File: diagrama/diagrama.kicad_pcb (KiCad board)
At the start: 2 copper layers, 160 x 101.6 mm, 13 parts, among them J1 Conn_01x02, U1 LM337_TO3

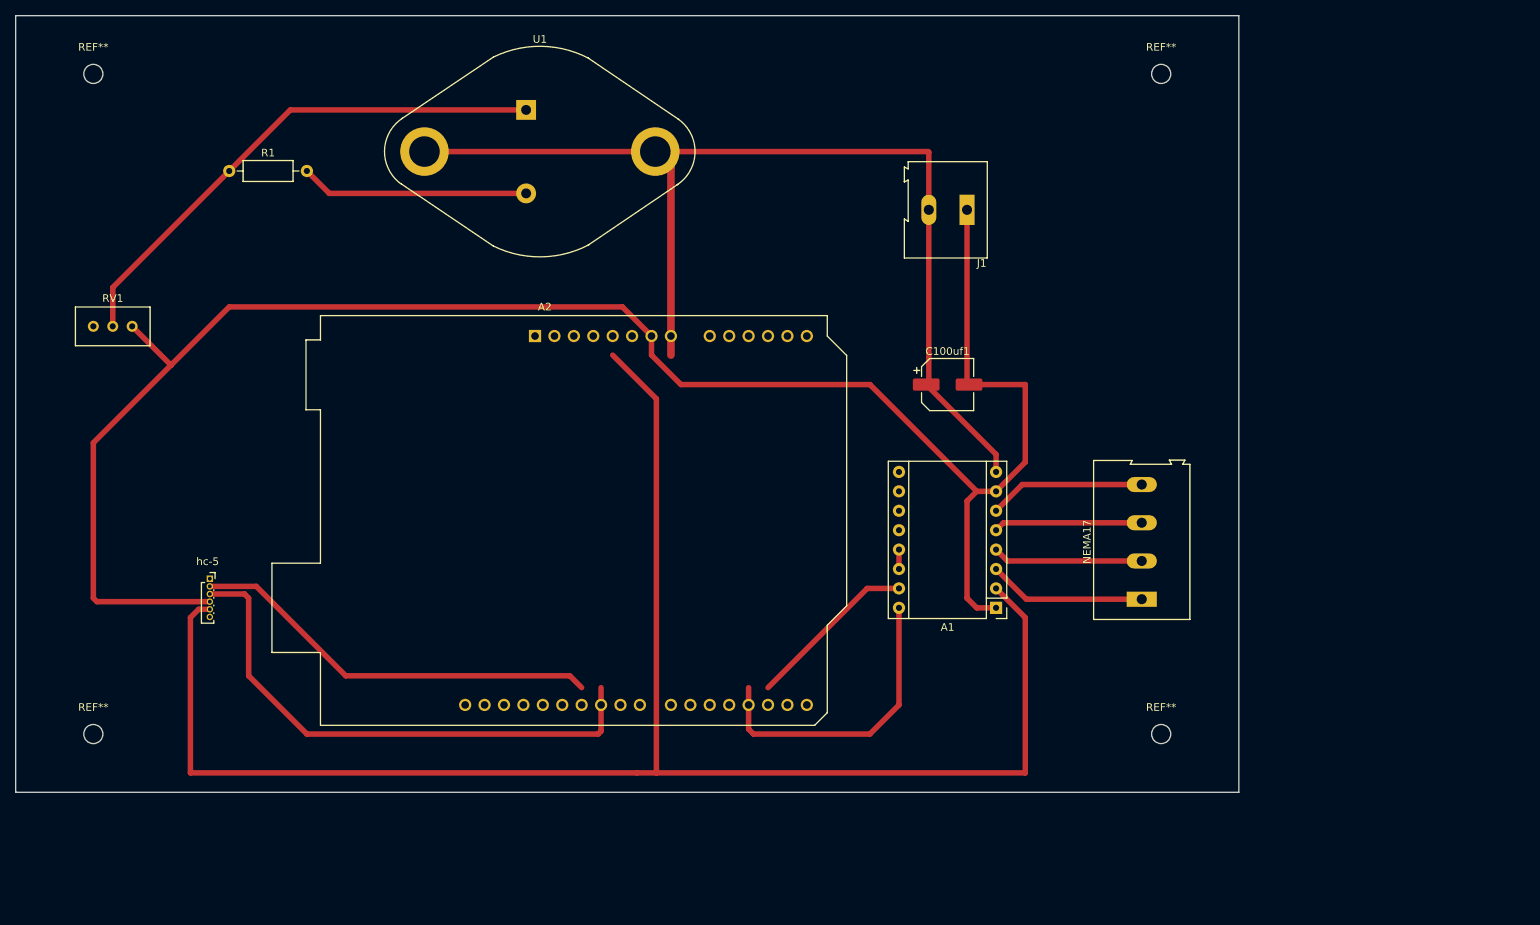
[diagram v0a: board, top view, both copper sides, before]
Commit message: eliminado input del ancho y muestra del progreso y cm en el lcd
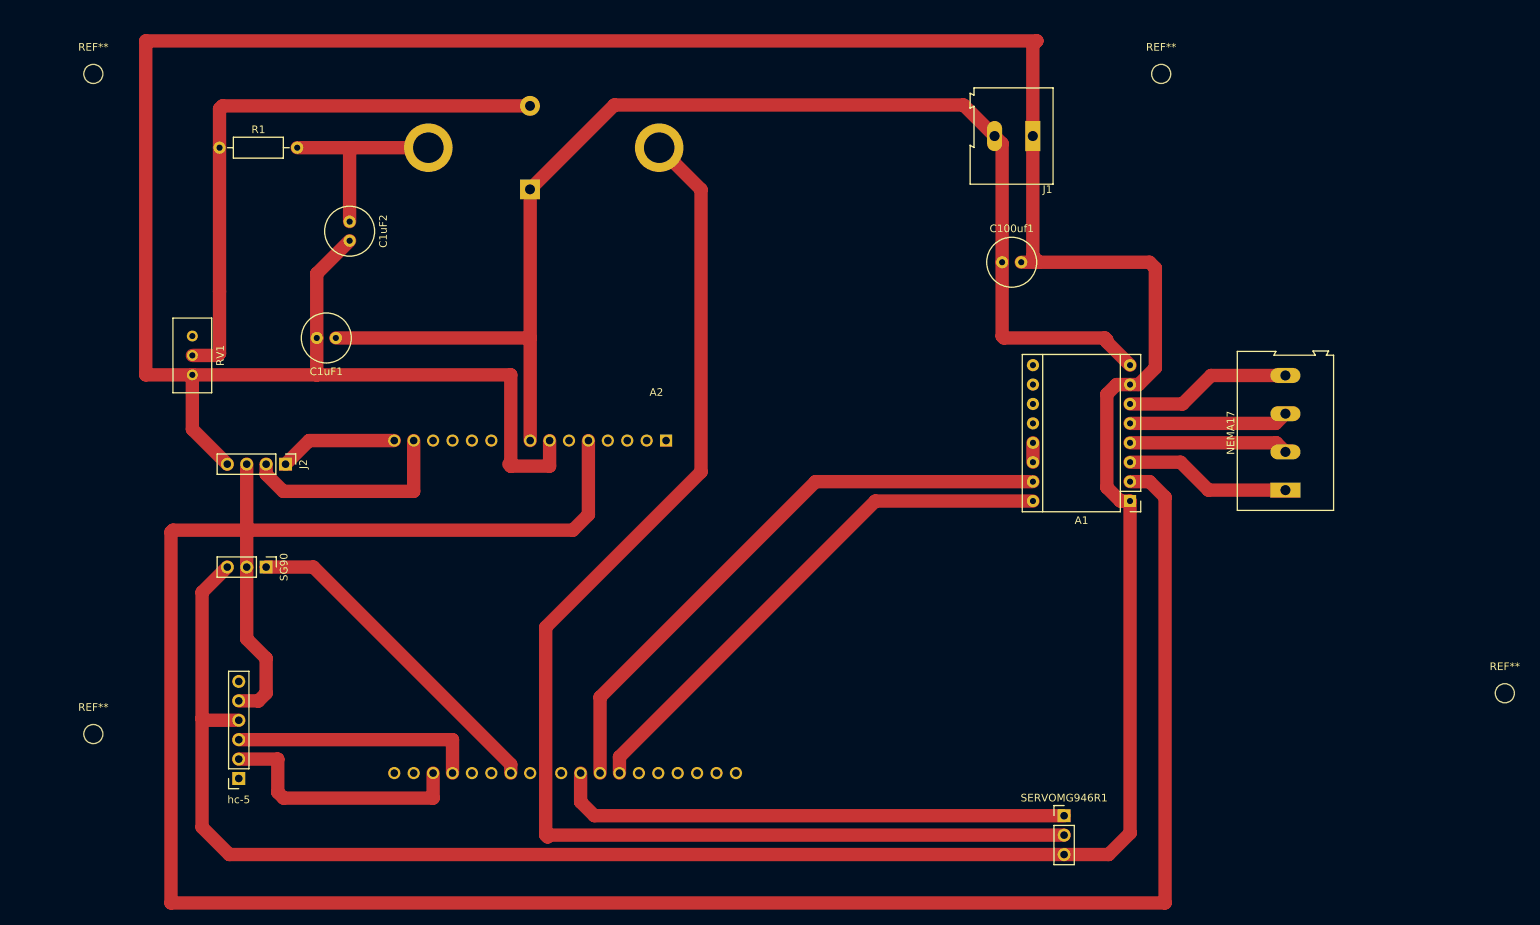
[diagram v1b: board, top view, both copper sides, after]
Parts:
- added C1uF1: C_Polarized, Capacitor_THT:C_Radial_D6.3mm_H11.0mm_P2.50mm, F.Cu at (85.1, 65.0)
- added C1uF2: C_Polarized, Capacitor_THT:C_Radial_D6.3mm_H11.0mm_P2.50mm, F.Cu at (86.9, 49.8)
- added J2: Conn_01x04_Male, Connector_PinHeader_2.54mm:PinHeader_1x04_P2.54mm_Vertical, F.Cu at (78.5, 81.5)
- added SERVOMG946R1: Conn_01x03_Male, Connector_PinHeader_2.54mm:PinHeader_1x03_P2.54mm_Vertical, F.Cu at (180.3, 127.5)
- added SG90: Conn_01x03_Male, Connector_PinHeader_2.54mm:PinHeader_1x03_P2.54mm_Vertical, F.Cu at (75.9, 95.0)
- A2: footprint Module:Arduino_UNO_R3 -> Module:Arduino_UNO_R3 modificado; moved to B.Cu
- C100uf1: footprint Capacitor_SMD:CP_Elec_6.3x9.9 -> Capacitor_THT:C_Radial_D6.3mm_H11.0mm_P2.50mm
- RV1: value R_Potentiometer -> R_Potentiometer 5K
- U1: footprint Package_TO_SOT_THT:TO-3 -> Package_TO_SOT_THT:TO-3-nuevo; moved to B.Cu
- hc-5: footprint Connector_PinSocket_1.00mm:PinSocket_1x06_P1.00mm_Vertical -> Connector_PinSocket_2.54mm:PinSocket_1x06_P2.54mm_Vertical
- moved REF** 45.3 mm to (238.0, 111.5)
- moved hc-5 26.4 mm to (72.4, 122.7), turned to 180 degrees
- moved NEMA17 23.6 mm to (209.3, 84.9)
- moved A1 22.4 mm to (189.0, 86.4)
- moved A2 20.5 mm to (128.3, 75.9), turned to 180 degrees
- moved C100uf1 17.5 mm to (172.2, 55.1)
- moved J1 12.9 mm to (176.2, 38.6)
- moved U1 10.4 mm to (110.5, 45.6)
- moved RV1 10.1 mm to (66.3, 69.8), turned to -90 degrees
- moved R1 3.30 mm to (69.8, 40.1)
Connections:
- net Net-(R1-Pad2) renamed 7V
- A2 pad 13: unconnected-(A2-Pad13) -> A4
- A2 pad 14: unconnected-(A2-Pad14) -> A5
- A2 pad 17: step -> Net-(A2-Pad17)
- A2 pad 18: dir -> Net-(A2-Pad18)
- A2 pad 21: unconnected-(A2-Pad21) -> SG90
- A2 pad 24: unconnected-(A2-Pad24) -> servo MG946R
- A2 pad 25: Net-(hc-5-Pad3) -> step
- A2 pad 26: Net-(hc-5-Pad2) -> dir
- A2 pad 6: unconnected-(A2-Pad6) -> GND
- hc-5 pad 2: Net-(hc-5-Pad2) -> Net-(A2-Pad17)
- hc-5 pad 3: Net-(hc-5-Pad3) -> Net-(A2-Pad18)
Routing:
- net GND: track 244.6 -> 553.7 mm
- net 7V: track 29.9 -> 195.6 mm
- net +5V: track 215.3 -> 337.4 mm
- net Net-(hc-5-Pad3): track 70.6 -> 0.00 mm
- net servo MG946R: track 0.00 -> 67.8 mm
- net step: track 22.5 -> 78.2 mm
- net Net-(hc-5-Pad2): track 54.1 -> 0.00 mm
- net SG90: track 0.00 -> 43.8 mm
- net Net-(A2-Pad17): track 0.00 -> 33.3 mm
- net Net-(A2-Pad18): track 0.00 -> 32.3 mm
- net +12V: track 139.3 -> 170.4 mm
- net dir: track 39.7 -> 70.1 mm
- net A4: track 0.00 -> 28.2 mm
- net A5: track 0.00 -> 15.5 mm
- net Net-(R1-Pad1): track 68.8 -> 76.4 mm
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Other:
- board outline removed
